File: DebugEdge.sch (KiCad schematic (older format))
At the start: 2 parts, among them J1 Upstream Host Connector, J2 DebugEdge_02x05

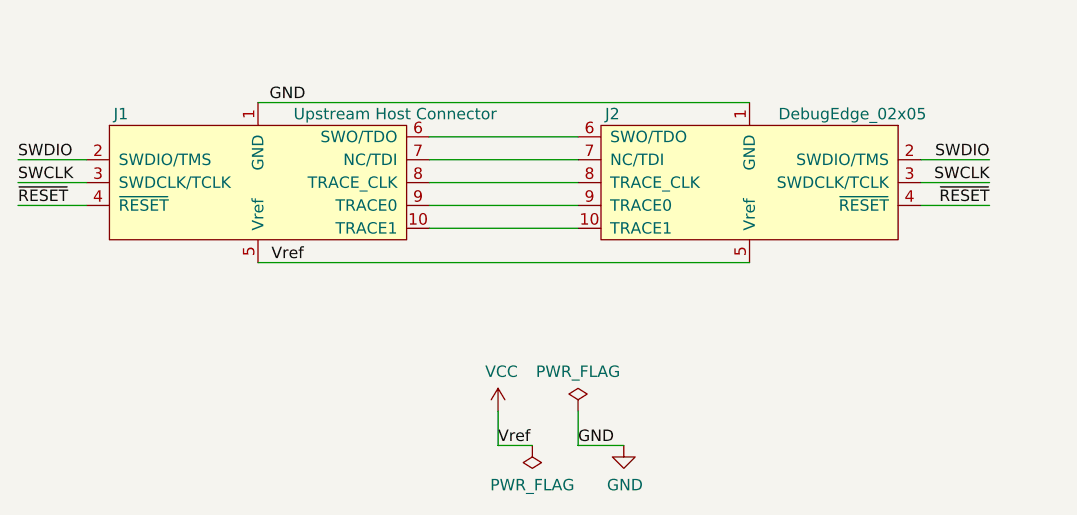
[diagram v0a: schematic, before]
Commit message: Add solder bridge for Vref & BYOP pins.
BYOP in case you need to bring your own power!
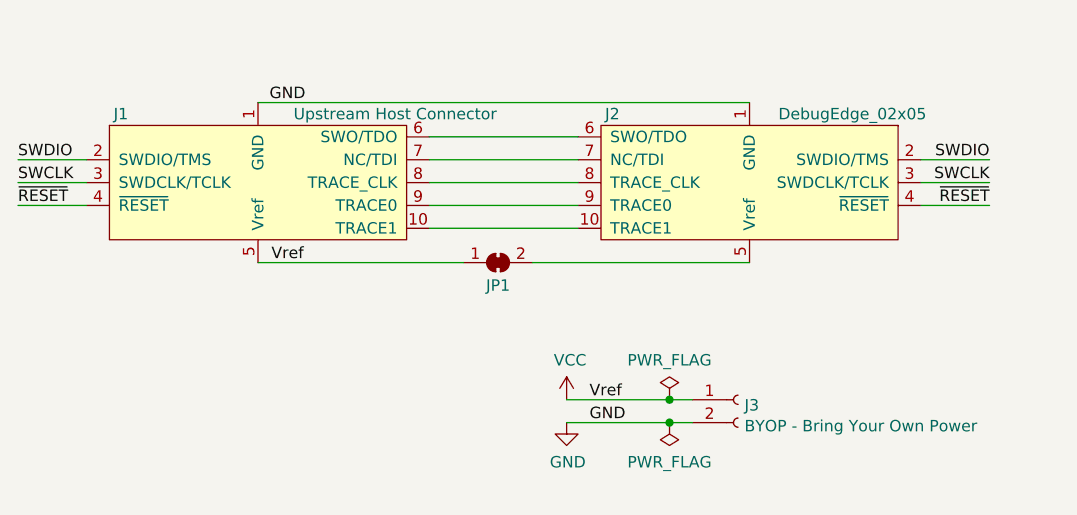
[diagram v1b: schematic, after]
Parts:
- added J3: BYOP - Bring Your Own Power, Connector_PinHeader_1.00mm:PinHeader_1x02_P1.00mm_Vertical, symbol Connector:Conn_01x02_Female
- added JP1: SolderJumper_2_Bridged, Jumper:SolderJumper-2_P1.3mm_Bridged_RoundedPad1.0x1.5mm, symbol Jumper:SolderJumper_2_Bridged
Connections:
- net GND: now also J3.2 (Pin_2)
- net VCC: now also J3.1 (Pin_1), JP1.1 (A); no longer J2.5 (Vref)
- new net: J2.5 (Vref), JP1.2 (B)
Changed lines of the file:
@@
 L power:GND #PWR0101
 U 1 1 5F46F758
-P 5650 4650
-F 0 "#PWR0101" H 5650 4400 50  0001 C CNN
-F 1 "GND" H 5655 4477 50  0000 C CNN
-F 2 "" H 5650 4650 50  0001 C CNN
-F 3 "" H 5650 4650 50  0001 C CNN
-	1    5650 4650
+P 5400 4550
+F 0 "#PWR0101" H 5400 4300 50  0001 C CNN
+F 1 "GND" H 5405 4377 50  0000 C CNN
+F 2 "" H 5400 4550 50  0001 C CNN
+F 3 "" H 5400 4550 50  0001 C CNN
+	1    5400 4550
 	1    0    0    -1
 $EndComp
-Wire Wire Line
-	5100 4500 5100 4650
-Wire Wire Line
-	5100 4650 5250 4650
-Wire Wire Line
-	5650 4650 5450 4650
-Wire Wire Line
-	5450 4650 5450 4500
 $Comp
 L power:PWR_FLAG #FLG0101
 U 1 1 5F47BD87
-P 5250 4650
-F 0 "#FLG0101" H 5250 4725 50  0001 C CNN
-F 1 "PWR_FLAG" H 5250 4823 50  0000 C CNN
-F 2 "" H 5250 4650 50  0001 C CNN
-F 3 "~" H 5250 4650 50  0001 C CNN
-	1    5250 4650
+P 5850 4550
+F 0 "#FLG0101" H 5850 4625 50  0001 C CNN
+F 1 "PWR_FLAG" H 5850 4723 50  0000 C CNN
+F 2 "" H 5850 4550 50  0001 C CNN
+F 3 "~" H 5850 4550 50  0001 C CNN
+	1    5850 4550
 	-1   0    0    1
 $EndComp
@@
 L power:PWR_FLAG #FLG0102
 U 1 1 5F47CF17
-P 5450 4500
-F 0 "#FLG0102" H 5450 4575 50  0001 C CNN
-F 1 "PWR_FLAG" H 5450 4673 50  0000 C CNN
-F 2 "" H 5450 4500 50  0001 C CNN
-F 3 "~" H 5450 4500 50  0001 C CNN
-	1    5450 4500
+P 5850 4450
+F 0 "#FLG0102" H 5850 4525 50  0001 C CNN
+F 1 "PWR_FLAG" H 5850 4623 50  0000 C CNN
+F 2 "" H 5850 4450 50  0001 C CNN
+F 3 "~" H 5850 4450 50  0001 C CNN
+	1    5850 4450
 	1    0    0    -1
 $EndComp
-Text Label 5450 4650 0    50   ~ 0
+Text Label 5500 4550 0    50   ~ 0
 GND
 $Comp
@@
 Text Label 4250 3850 2    50   ~ 0
 Vref
-Text Label 5100 4650 0    50   ~ 0
+Text Label 5500 4450 0    50   ~ 0
 Vref
 $Comp
 L power:VCC #PWR01
 U 1 1 5F46D625
-P 5100 4500
-F 0 "#PWR01" H 5100 4350 50  0001 C CNN
-F 1 "VCC" H 5115 4673 50  0000 C CNN
-F 2 "" H 5100 4500 50  0001 C CNN
-F 3 "" H 5100 4500 50  0001 C CNN
-	1    5100 4500
+P 5400 4450
+F 0 "#PWR01" H 5400 4300 50  0001 C CNN
+F 1 "VCC" H 5415 4623 50  0000 C CNN
+F 2 "" H 5400 4450 50  0001 C CNN
+F 3 "" H 5400 4450 50  0001 C CNN
+	1    5400 4450
 	1    0    0    -1
 $EndComp
@@
 	5450 3700 4800 3700
 Wire Wire Line
-	6200 3850 4050 3850
-Wire Wire Line
 	4050 3150 6200 3150
 Wire Wire Line
@@
 Text Label 3000 3500 0    50   ~ 0
 SWCLK
+$Comp
+L Jumper:SolderJumper_2_Bridged JP1
+U 1 1 5F47209A
+P 5100 3850
+F 0 "JP1" H 5100 3750 50  0000 C CNN
+F 1 "SolderJumper_2_Bridged" H 5100 3964 50  0001 C CNN
+F 2 "Jumper:SolderJumper-2_P1.3mm_Bridged_RoundedPad1.0x1.5mm" H 5100 3850 50  0001 C CNN
+F 3 "~" H 5100 3850 50  0001 C CNN
+	1    5100 3850
+	1    0    0    -1
+$EndComp
+Wire Wire Line
+	4050 3850 4950 3850
+Wire Wire Line
+	5250 3850 6200 3850
+$Comp
+L Connector:Conn_01x02_Female J3
+U 1 1 5F4762C8
+P 6150 4450
+F 0 "J3" H 6178 4426 50  0000 L CNN
+F 1 "BYOP - Bring Your Own Power" H 6178 4335 50  0000 L CNN
+F 2 "Connector_PinHeader_1.00mm:PinHeader_1x02_P1.00mm_Vertical" H 6150 4450 50  0001 C CNN
+F 3 "~" H 6150 4450 50  0001 C CNN
+	1    6150 4450
+	1    0    0    -1
+$EndComp
+Wire Wire Line
+	5950 4450 5850 4450
+Connection ~ 5850 4450
+Connection ~ 5850 4550
+Wire Wire Line
+	5850 4550 5950 4550
+Wire Wire Line
+	5400 4450 5850 4450
+Wire Wire Line
+	5400 4550 5850 4550
 $EndSCHEMATC

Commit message: Update host adapter to new footprint
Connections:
- net TRACE1: now reaches J1.10 (TRACE1), J2.10 (TRACE1)
- net SWO_TDO: now reaches J1.6 (SWO/TDO), J2.6 (SWO/TDO)
- net TDI: now reaches J1.7 (NC/TDI), J2.7 (NC/TDI)
- net TRACE_CLK: now reaches J1.8 (TRACE_CLK), J2.8 (TRACE_CLK)
- net TRACE0: now reaches J1.9 (TRACE0), J2.9 (TRACE0)
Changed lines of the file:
@@
 $Descr A4 11693 8268
 encoding utf-8
-Sheet 1 2
+Sheet 1 1
 Title "DebugEdge SWD Adapter"
 Date "2020-08-27"
@@
 Wire Wire Line
 	5400 4550 5850 4550
+Text Label 5050 3300 0    50   ~ 0
+SWO_TDO
+Text Label 5050 3400 0    50   ~ 0
+TDI
+Text Label 5050 3500 0    50   ~ 0
+TRACE_CLK
+Text Label 5050 3600 0    50   ~ 0
+TRACE0
+Text Label 5050 3700 0    50   ~ 0
+TRACE1
 $EndSCHEMATC

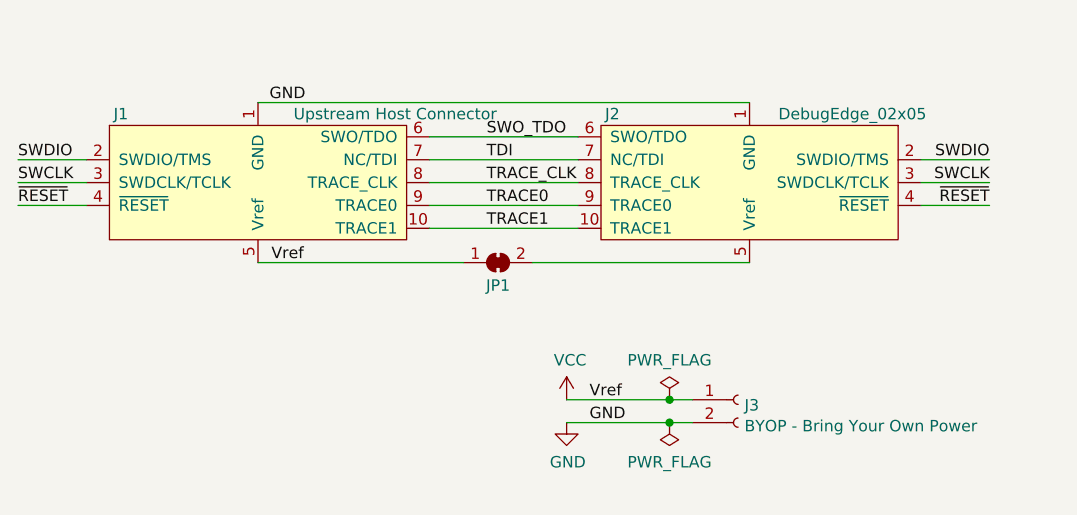
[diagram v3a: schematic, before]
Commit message: change 2x5 adapter to swd/jtag pinout
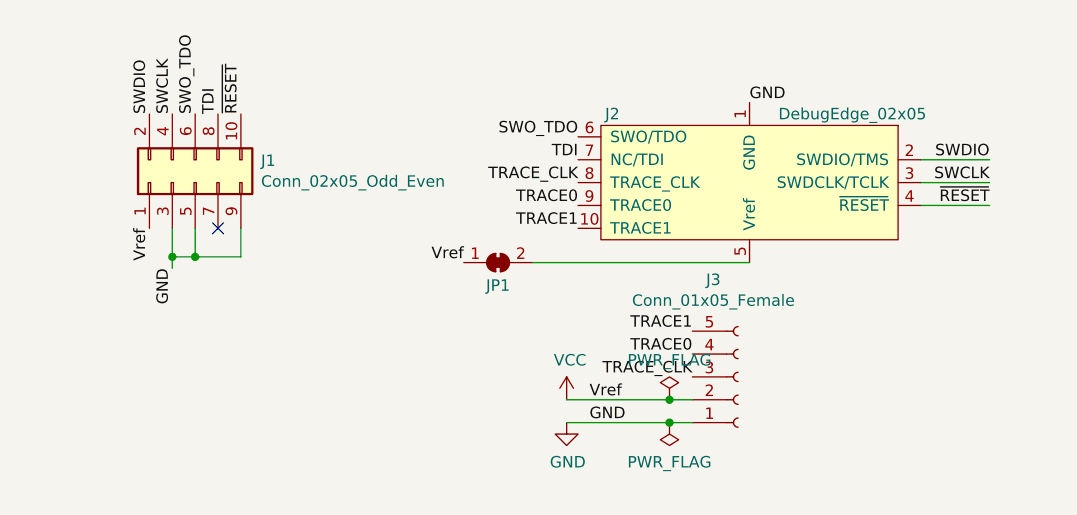
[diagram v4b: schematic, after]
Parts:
- removed J1: Upstream Host Connector, Connector_PinHeader_1.27mm:PinHeader_2x05_P1.27mm_Vertical_SMD, symbol Connector_DebugEdge:DebugEdge_02x05
- removed J3: BYOP - Bring Your Own Power, Connector_PinHeader_1.00mm:PinHeader_1x02_P1.00mm_Vertical, symbol Connector:Conn_01x02_Female
- added J1: Conn_02x05_Odd_Even, Connector_PinHeader_1.27mm:PinHeader_2x05_P1.27mm_Vertical_SMD, symbol Connector_Generic:Conn_02x05_Odd_Even
- added J3: Conn_01x05_Female, Connector_PinSocket_2.54mm:PinSocket_1x05_P2.54mm_Vertical, symbol Connector:Conn_01x05_Female
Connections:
- net GND: now also J1.3 (Pin_3), J1.5 (Pin_5), J1.9 (Pin_9), J3.1 (Pin_1)
- net SWCLK: now also J1.4 (Pin_4)
- net SWDIO: now also J1.2 (Pin_2)
- net SWO_TDO: now also J1.6 (Pin_6)
- net TDI: now also J1.8 (Pin_8)
- net TRACE0: now also J3.4 (Pin_4)
- net TRACE1: now also J3.5 (Pin_5)
- net TRACE_CLK: now also J3.3 (Pin_3)
- net VCC: now also J1.1 (Pin_1), J3.2 (Pin_2)
- net ~RESET~: now also J1.10 (Pin_10)
- no-connect marks 0 -> 1
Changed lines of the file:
@@
 $EndDescr
-Wire Wire Line
-	3300 3600 3000 3600
 Wire Wire Line
 	6950 3500 7250 3500
 Wire Wire Line
 	6950 3400 7250 3400
-Text Label 4100 3150 0    50   ~ 0
+Text Label 3675 3875 3    50   ~ 0
 GND
 Text Label 7250 3400 2    50   ~ 0
@@
 Text Label 7250 3500 2    50   ~ 0
 SWCLK
-Text Label 3000 3600 0    50   ~ 0
+Text Label 3975 3200 1    50   ~ 0
 ~RESET~
 $Comp
@@
 	-1   0    0    -1
 $EndComp
-Text Label 4250 3850 2    50   ~ 0
+Text Label 3575 3700 3    50   ~ 0
 Vref
 Text Label 5500 4450 0    50   ~ 0
@@
 	1    0    0    -1
 $EndComp
-$Comp
-L Connector_DebugEdge:DebugEdge_02x05 J1
-U 1 1 5F47310F
-P 4050 3500
-F 0 "J1" H 3450 3800 50  0000 C CNN
-F 1 "Upstream Host Connector" H 4650 3800 50  0000 C CNN
-F 2 "Connector_PinHeader_1.27mm:PinHeader_2x05_P1.27mm_Vertical_SMD" H 4050 3900 50  0001 C CNN
-F 3 "" H 4050 3900 50  0001 C CNN
-	1    4050 3500
-	1    0    0    -1
-$EndComp
-Wire Wire Line
-	5450 3300 4800 3300
-Wire Wire Line
-	5450 3400 4800 3400
-Wire Wire Line
-	5450 3500 4800 3500
-Wire Wire Line
-	5450 3600 4800 3600
-Wire Wire Line
-	5450 3700 4800 3700
-Wire Wire Line
-	4050 3150 6200 3150
 Wire Wire Line
 	6950 3600 7250 3600
 Text Label 7250 3600 2    50   ~ 0
 ~RESET~
-Wire Wire Line
-	3300 3400 3000 3400
-Wire Wire Line
-	3300 3500 3000 3500
-Text Label 3000 3400 0    50   ~ 0
+Text Label 3575 3200 1    50   ~ 0
 SWDIO
-Text Label 3000 3500 0    50   ~ 0
+Text Label 3675 3200 1    50   ~ 0
 SWCLK
 $Comp
@@
 $EndComp
 Wire Wire Line
-	4050 3850 4950 3850
-Wire Wire Line
 	5250 3850 6200 3850
-$Comp
-L Connector:Conn_01x02_Female J3
-U 1 1 5F4762C8
-P 6150 4450
-F 0 "J3" H 6178 4426 50  0000 L CNN
-F 1 "BYOP - Bring Your Own Power" H 6178 4335 50  0000 L CNN
-F 2 "Connector_PinHeader_1.00mm:PinHeader_1x02_P1.00mm_Vertical" H 6150 4450 50  0001 C CNN
-F 3 "~" H 6150 4450 50  0001 C CNN
-	1    6150 4450
-	1    0    0    -1
-$EndComp
 Wire Wire Line
 	5950 4450 5850 4450
@@
 Wire Wire Line
 	5400 4550 5850 4550
-Text Label 5050 3300 0    50   ~ 0
+Text Label 5450 3300 2    50   ~ 0
 SWO_TDO
-Text Label 5050 3400 0    50   ~ 0
+Text Label 5450 3400 2    50   ~ 0
 TDI
-Text Label 5050 3500 0    50   ~ 0
+Text Label 5450 3500 2    50   ~ 0
 TRACE_CLK
-Text Label 5050 3600 0    50   ~ 0
+Text Label 5450 3600 2    50   ~ 0
 TRACE0
-Text Label 5050 3700 0    50   ~ 0
+Text Label 5450 3700 2    50   ~ 0
+TRACE1
+$Comp
+L Connector_Generic:Conn_02x05_Odd_Even J1
+U 1 1 5FA470BD
+P 3775 3500
+F 0 "J1" V 3871 3212 50  0000 R CNN
+F 1 "Conn_02x05_Odd_Even" V 3780 3212 50  0000 R CNN
+F 2 "Connector_PinHeader_1.27mm:PinHeader_2x05_P1.27mm_Vertical_SMD" H 3775 3500 50  0001 C CNN
+F 3 "~" H 3775 3500 50  0001 C CNN
+	1    3775 3500
+	0    -1   -1   0
+$EndComp
+Text Label 4950 3850 2    50   ~ 0
+Vref
+Wire Wire Line
+	3675 3700 3675 3825
+Wire Wire Line
+	3975 3700 3975 3825
+Wire Wire Line
+	3975 3825 3775 3825
+Connection ~ 3675 3825
+Wire Wire Line
+	3675 3825 3675 3875
+Wire Wire Line
+	3775 3700 3775 3825
+Connection ~ 3775 3825
+Wire Wire Line
+	3775 3825 3675 3825
+NoConn ~ 3875 3700
+Text Label 3775 3200 1    50   ~ 0
+SWO_TDO
+Text Label 3875 3200 1    50   ~ 0
+TDI
+Text Label 6200 3150 0    50   ~ 0
+GND
+$Comp
+L Connector:Conn_01x05_Female J3
+U 1 1 5FA5524C
+P 6150 4350
+F 0 "J3" H 6042 3925 50  0000 C CNN
+F 1 "Conn_01x05_Female" H 6042 4016 50  0000 C CNN
+F 2 "Connector_PinSocket_2.54mm:PinSocket_1x05_P2.54mm_Vertical" H 6150 4350 50  0001 C CNN
+F 3 "~" H 6150 4350 50  0001 C CNN
+	1    6150 4350
+	1    0    0    1
+$EndComp
+Text Label 5950 4350 2    50   ~ 0
+TRACE_CLK
+Text Label 5950 4250 2    50   ~ 0
+TRACE0
+Text Label 5950 4150 2    50   ~ 0
 TRACE1
 $EndSCHEMATC
